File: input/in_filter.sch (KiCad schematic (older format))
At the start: 36 parts

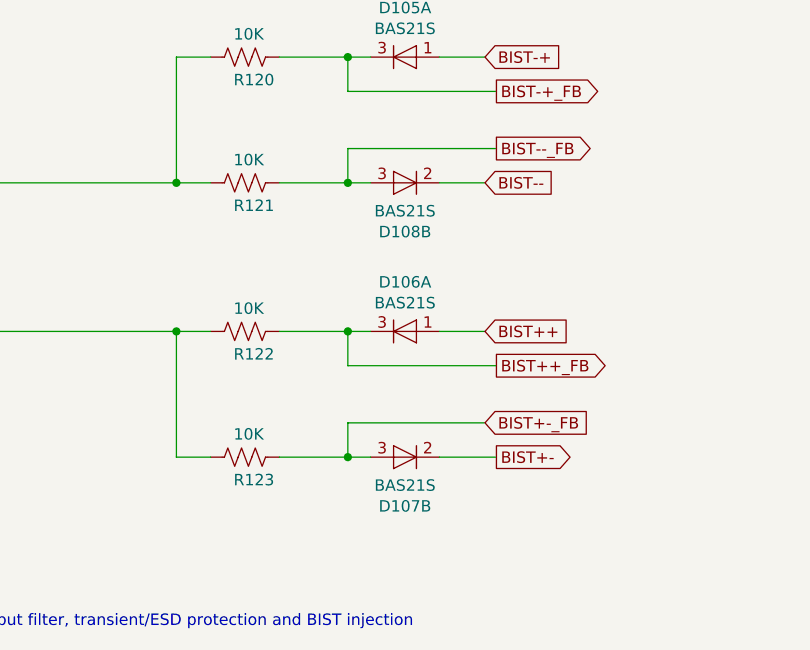
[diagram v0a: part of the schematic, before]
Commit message: Changed board connector to PCIe 8x, added test points, cleanup of component values. Add LVDS Rx termination, bypass caps.
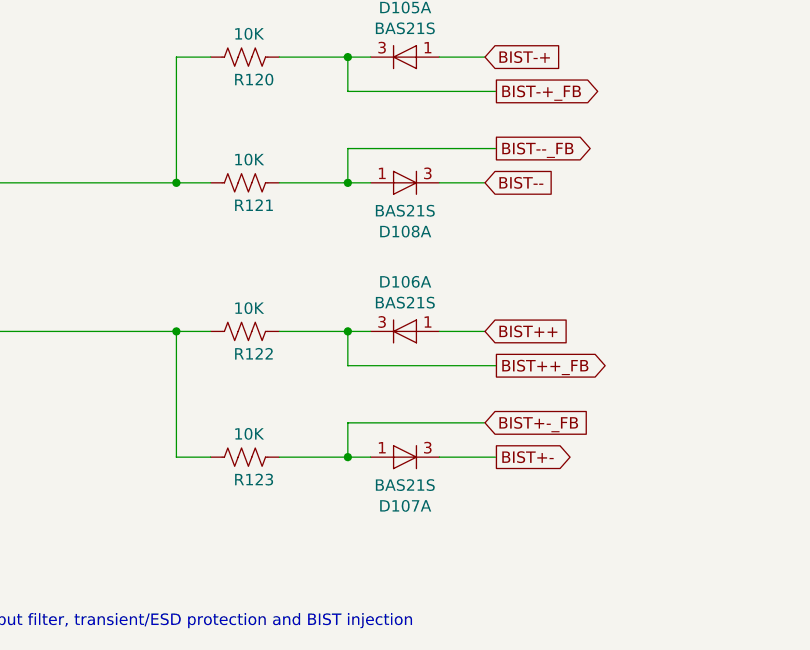
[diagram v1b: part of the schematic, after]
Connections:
- net BIST+-: now also D107.3 (K); no longer D107.2 (K)
- net BIST+-_FB: now also D107.1 (A); no longer D107.3 (A)
- net BIST--: now also D108.3 (K); no longer D108.2 (K)
- net BIST--_FB: now also D108.1 (A); no longer D108.3 (A)
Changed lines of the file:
@@
 $Comp
 L ilemt_input:BAS21S D108
-U 2 1 5E1955BE
+U 1 1 5E1955BE
 P 8900 4800
 F 0 "D108" H 8900 5015 50  0000 C CNN
@@
 F 2 "Package_TO_SOT_SMD:SOT-23" H 8900 4650 50  0001 C CNN
 F 3 "https://assets.nexperia.com/documents/data-sheet/BAV99_SER.pdf" H 8900 4900 50  0001 C CNN
-	2    8900 4800
+	1    8900 4800
 	-1   0    0    1
 $EndComp
@@
 $Comp
 L ilemt_input:BAS21S D107
-U 2 1 5E1955C0
+U 1 1 5E1955C0
 P 8900 6000
 F 0 "D107" H 8900 6215 50  0000 C CNN
@@
 F 2 "Package_TO_SOT_SMD:SOT-23" H 8900 5850 50  0001 C CNN
 F 3 "https://assets.nexperia.com/documents/data-sheet/BAV99_SER.pdf" H 8900 6100 50  0001 C CNN
-	2    8900 6000
+	1    8900 6000
 	-1   0    0    1
 $EndComp

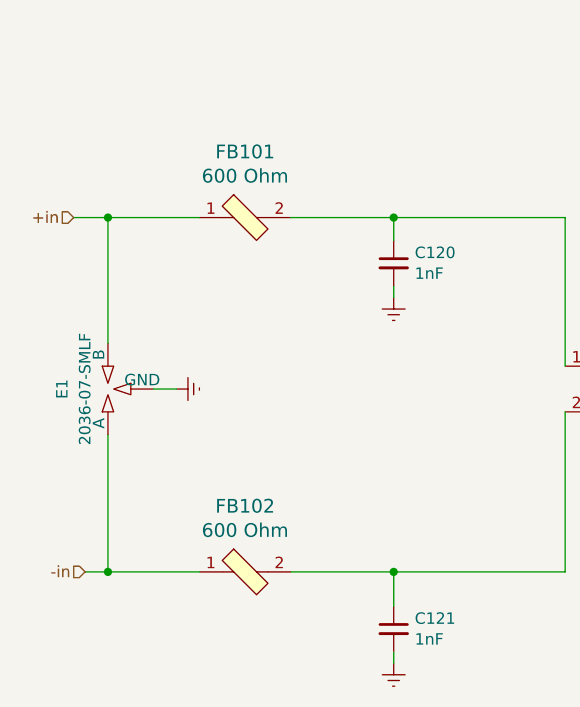
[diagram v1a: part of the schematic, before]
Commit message: Checkpoint before starting routing.  Added power and ground testpoints.
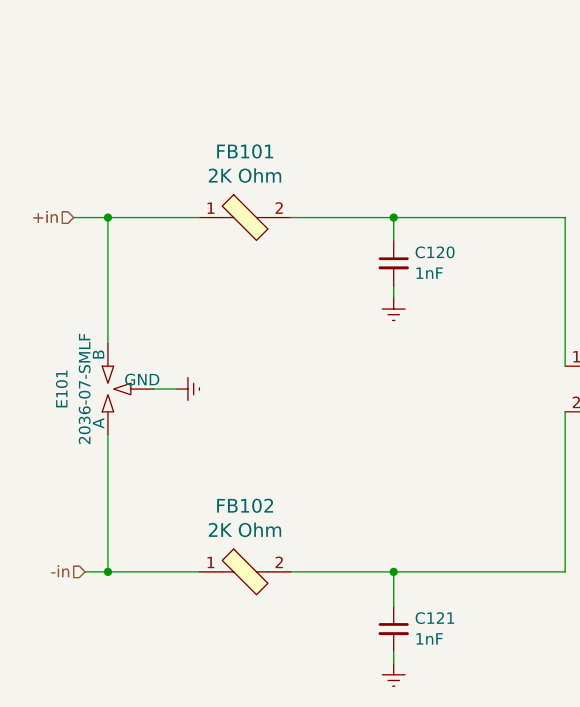
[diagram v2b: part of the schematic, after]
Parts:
- C120, C121, C127, C128: DK line (none) -> 1; Description (none) -> CAP CER 1000PF 100V NPO 0805
- C122: footprint Capacitor_SMD:C_0603_1608Metric -> Capacitor_SMD:C_0805_2012Metric; DK line (none) -> 45; Description (none) -> 3300pF ±5% 50V Ceramic Capacitor C0G, NP0 0805 (2012 Metric); Digikey (none) -> 311-4211-1-ND
- C123, C124, C125, C126: DK line (none) -> 27
- D101, D102: DK line (none) -> 7; Description (none) -> TVS DIODE 12V 35V SOD323
- D103, D104, D105, D106, D107, D108: DK line (none) -> 43; Description (none) -> DIODE ARRAY GP 250V 225MA SOT23; Digikey (none) -> BAS21SLT1GOSCT-ND; MPN (none) -> BAS21SLT1G
- E101: renamed from E1; DK line (none) -> 8
- FB101, FB102: value 600 Ohm -> 2K Ohm; DK line (none) -> 5; Description FERRITE BEAD 600 OHM 0805 1LN -> FERRITE BEAD 2 KOHM 0805 1LN; Digikey (none) -> 240-2396-1-ND
- FL101: DK line (none) -> 6; Description (none) -> CMC 4.7MH 200MA 2LN SMD
- R113, R114, R131, R132: DK line (none) -> 54; Description (none) -> 200 kOhms ±1% 0.1W, 1/10W Chip Resistor 0603 (1608 Metric) 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; Digikey (none) -> YAG5945CT-ND
- R115, R116, R117, R118, R124, R125: DK line (none) -> 9; Description (none) -> RES SMD 10 OHM 5% 1/2W 0805
- R119: DK line (none) -> 55; Description (none) -> 200 Ohms ±1% 0.125W, 1/8W Chip Resistor 0603 (1608 Metric) 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; Digikey (none) -> RNCP0603FTD200RCT-ND
- R120, R121, R122, R123: DK line (none) -> 56; Description (none) -> RES SMD 10K OHM 0.1% 1/10W 0603; Digikey (none) -> P10KDBCT-ND

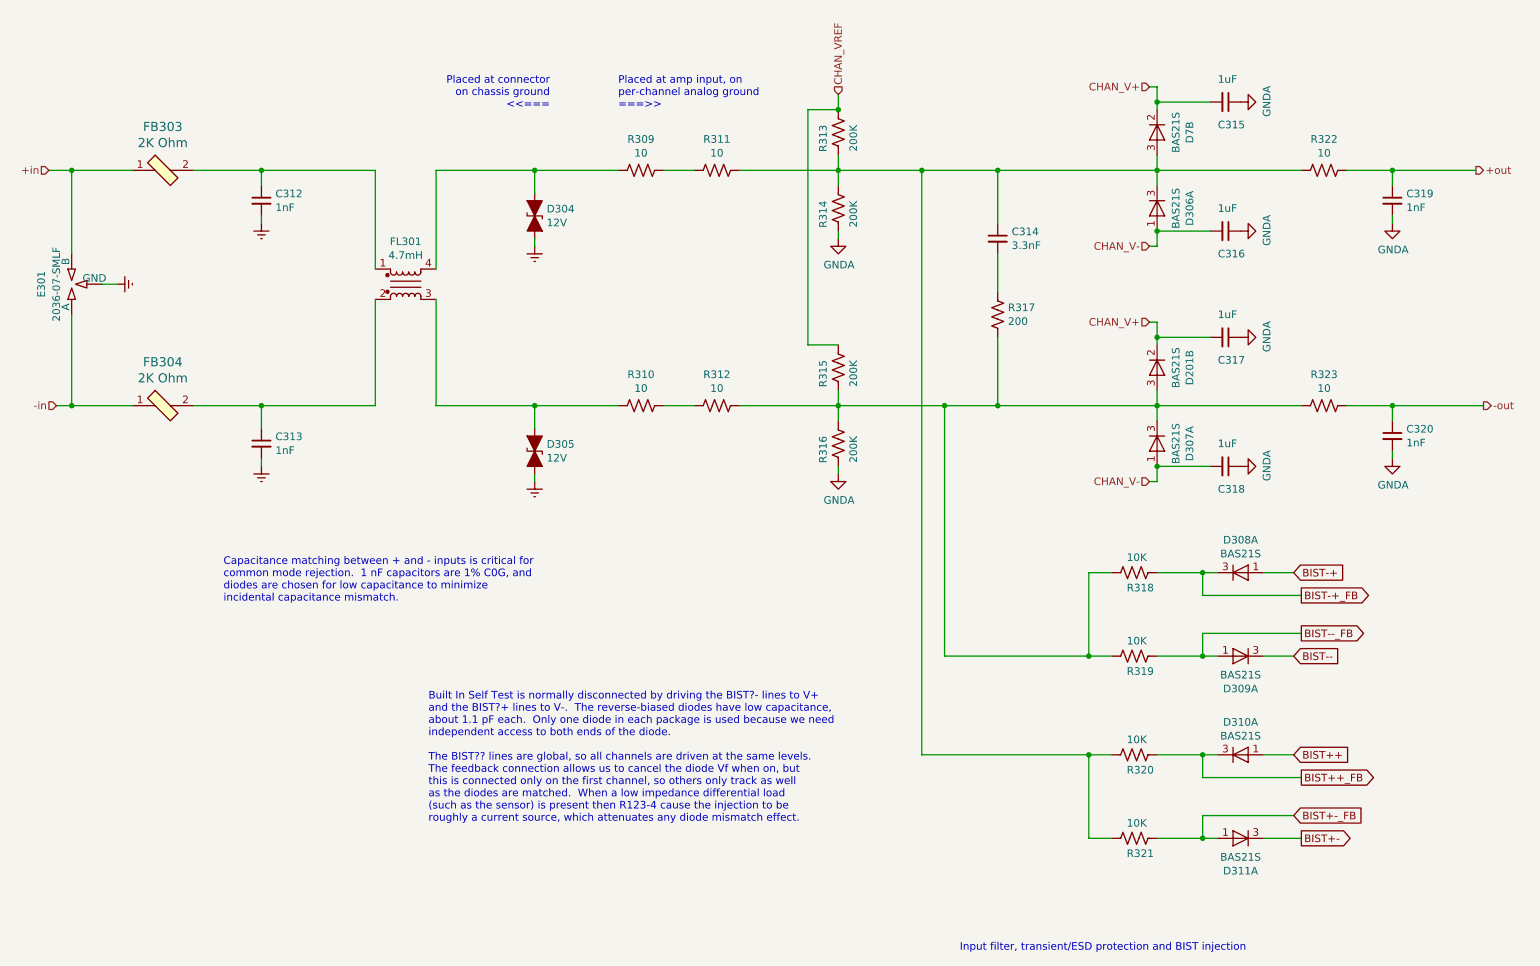
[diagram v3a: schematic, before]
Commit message: Input board is nearly ready to send off for the first spin.
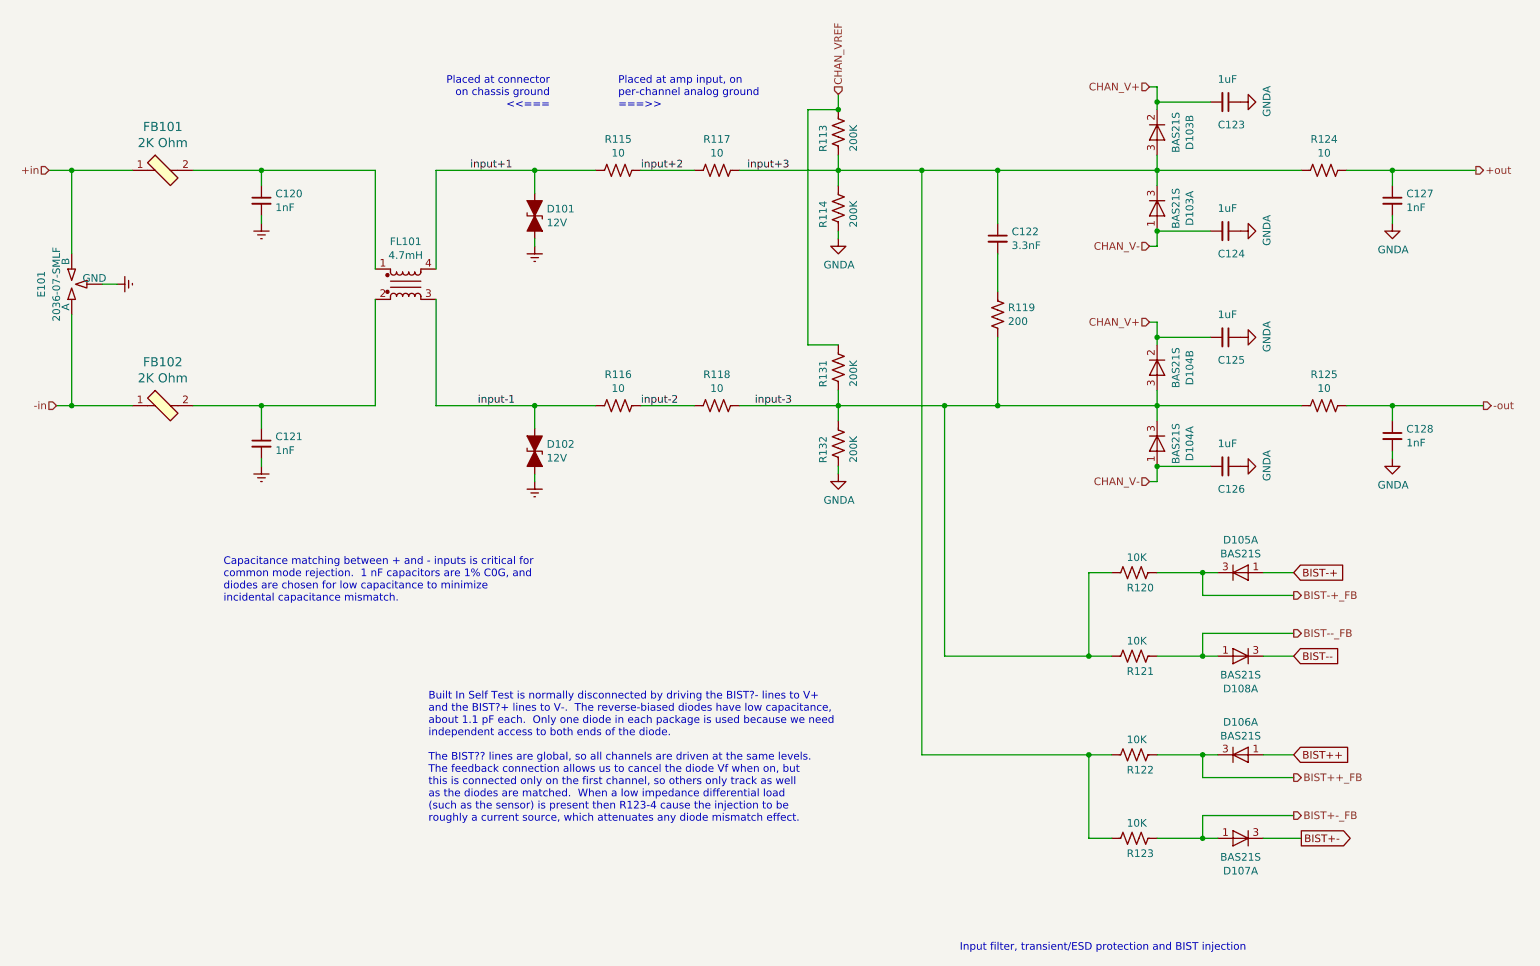
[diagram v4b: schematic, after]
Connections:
- net input+3: now reaches C122.1, D103.3 (A), D103.3 (K), R113.1, R114.2, R117.1, R122.2, R123.2, R124.2
- net input-3: now reaches D104.3 (A), D104.3 (K), R118.1, R119.2, R120.2, R121.2, R125.2, R131.1, R132.2
- net input+2: now reaches R115.1, R117.2
- net input-2: now reaches R116.1, R118.2
- net input+1: now reaches D101.1 (A1), FL101.4, R115.2
- net input-1: now reaches D102.1 (A1), FL101.3, R116.2
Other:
- moved on the sheet: R115, R116

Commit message: Changed the input TVS from 12V bidirectional to 8V unidirectional, board tweaks
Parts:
- D101, D102: value 12V -> 8V; symbol Device:D_TVS_ALT -> Device:D_Zener_ALT; DK line 7 -> 58; Description TVS DIODE 12V 35V SOD323 -> TVS DIODE 8V 18.3V SOD323; Digikey F10399CT-ND -> CDSOD323-T08LCT-ND; MPN AQ4022-01FTG-C -> CDSOD323-T08L
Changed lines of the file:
@@
 	8350 1500 8350 1600
 $Comp
-L Device:D_TVS_ALT D101
+L Device:D_Zener_ALT D101
 U 1 1 5DE60CD7
 P 4250 1900
@@
 AR Path="/5E45936E/5DE42731/5DE60CD7" Ref="D304"  Part="1"
 F 0 "D101" V 4204 1979 50  0000 L CNN
-F 1 "12V" V 4295 1979 50  0000 L CNN
+F 1 "8V" V 4295 1979 50  0000 L CNN
 F 2 "Diode_SMD:D_SOD-323" H 4250 1900 50  0001 C CNN
 F 3 "https://www.littelfuse.com/~/media/electronics/datasheets/tvs_diode_arrays/littelfuse_tvs_diode_array_aq4022_datasheet.pdf" H 4250 1900 50  0001 C CNN
-F 4 "F10399CT-ND" V 4250 1900 50  0001 C CNN "Digikey"
-F 5 "AQ4022-01FTG-C" V 4250 1900 50  0001 C CNN "MPN"
-F 6 "7" H 4250 1900 50  0001 C CNN "DK line"
-F 7 "TVS DIODE 12V 35V SOD323" H 4250 1900 50  0001 C CNN "Description"
+F 4 "CDSOD323-T08LCT-ND" V 4250 1900 50  0001 C CNN "Digikey"
+F 5 "CDSOD323-T08L" V 4250 1900 50  0001 C CNN "MPN"
+F 6 "58" H 4250 1900 50  0001 C CNN "DK line"
+F 7 "TVS DIODE 8V 18.3V SOD323" H 4250 1900 50  0001 C CNN "Description"
 	1    4250 1900
 	0    1    1    0
@@
 	8350 3050 8350 3150
 $Comp
-L Device:D_TVS_ALT D102
+L Device:D_Zener_ALT D102
 U 1 1 5DE6E14A
 P 4250 3450
@@
 AR Path="/5E45936E/5DE42731/5DE6E14A" Ref="D305"  Part="1"
 F 0 "D102" V 4204 3529 50  0000 L CNN
-F 1 "12V" V 4295 3529 50  0000 L CNN
+F 1 "8V" V 4295 3529 50  0000 L CNN
 F 2 "Diode_SMD:D_SOD-323" H 4250 3450 50  0001 C CNN
 F 3 "https://www.littelfuse.com/~/media/electronics/datasheets/tvs_diode_arrays/littelfuse_tvs_diode_array_aq4022_datasheet.pdf" H 4250 3450 50  0001 C CNN
-F 4 "F10399CT-ND" V 4250 3450 50  0001 C CNN "Digikey"
-F 5 "AQ4022-01FTG-C" V 4250 3450 50  0001 C CNN "MPN"
-F 6 "7" H 4250 3450 50  0001 C CNN "DK line"
-F 7 "TVS DIODE 12V 35V SOD323" H 4250 3450 50  0001 C CNN "Description"
+F 4 "CDSOD323-T08LCT-ND" V 4250 3450 50  0001 C CNN "Digikey"
+F 5 "CDSOD323-T08L" V 4250 3450 50  0001 C CNN "MPN"
+F 6 "58" H 4250 3450 50  0001 C CNN "DK line"
+F 7 "TVS DIODE 8V 18.3V SOD323" H 4250 3450 50  0001 C CNN "Description"
 	1    4250 3450
 	0    1    1    0

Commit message: Checkpoint of state before I start schematic revisions for the next version of the input board. There are not any substantive modifications to the input board, but some broad changes in component attributes related enabling a fabrication quote.
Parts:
- C120, C121, C127, C128: Manufacturer (none) -> Yageo
- C122: MPN (none) -> CC0805JKNPO9BN332; Manufacturer (none) -> Yageo
- C123, C124, C125, C126: Manufacturer (none) -> Samsung Electro-Mechanics
- D101, D102, FL101: Manufacturer (none) -> Bourns Inc.
- D103, D104, D105, D106, D107, D108: Manufacturer (none) -> ON Semiconductor
- E101: MPN (none) -> 2036-07-SMLF; Manufacturer (none) -> Bourns Inc.
- FB101, FB102: Manufacturer TDK Corporation -> Laird-Signal Integrity Products
- R113, R114, R131, R132: MPN (none) -> RT0603FRE07200KL; Manufacturer (none) -> Yageo
- R115, R116, R117, R118, R124, R125: Manufacturer (none) -> Vishay Dale
- R119: MPN (none) -> RNCP0603FTD200R; Manufacturer (none) -> Stackpole Electronics Inc
- R120, R121, R122, R123: MPN (none) -> ERA-3AEB103V; Manufacturer (none) -> Panasonic Electronic Components
